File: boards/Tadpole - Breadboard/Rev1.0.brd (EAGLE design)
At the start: 57 x 50 mm, 8 parts

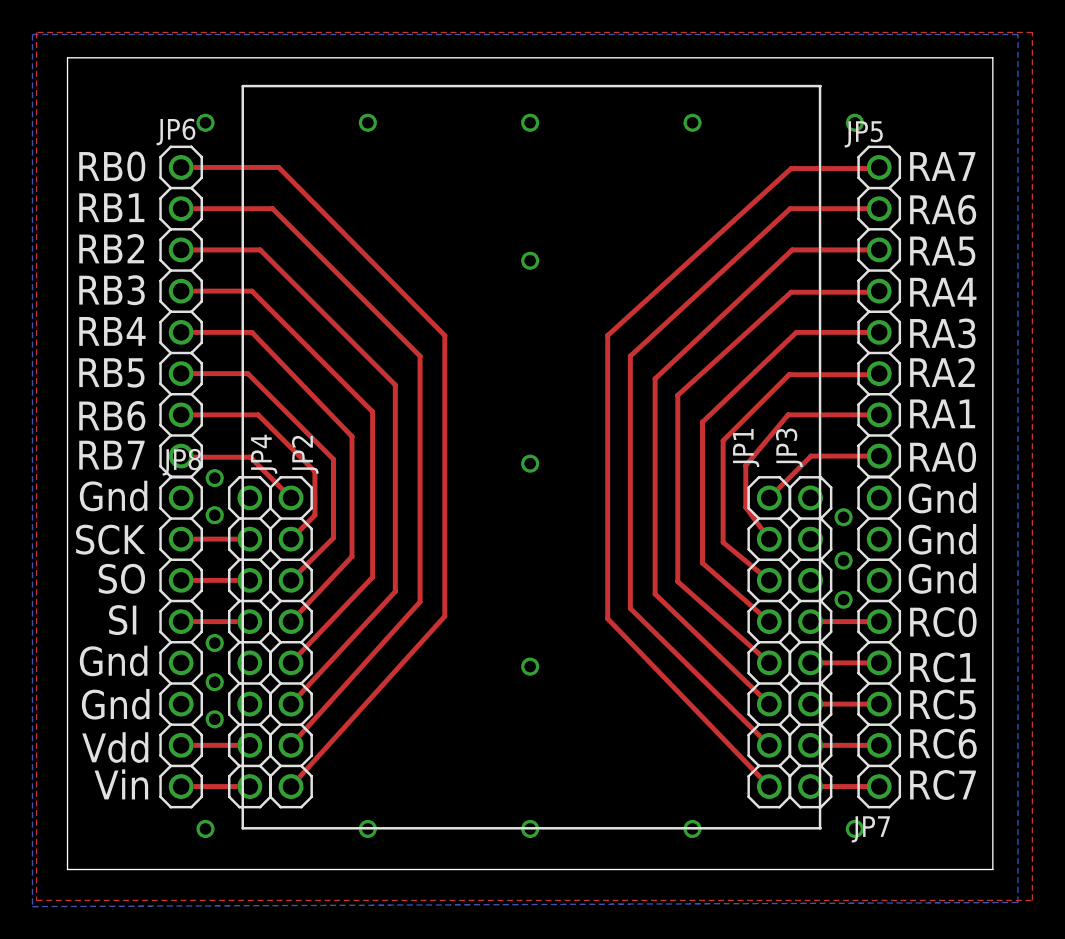
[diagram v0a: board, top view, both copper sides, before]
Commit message: Kermit PIC protocol and small frogbrain board mods.
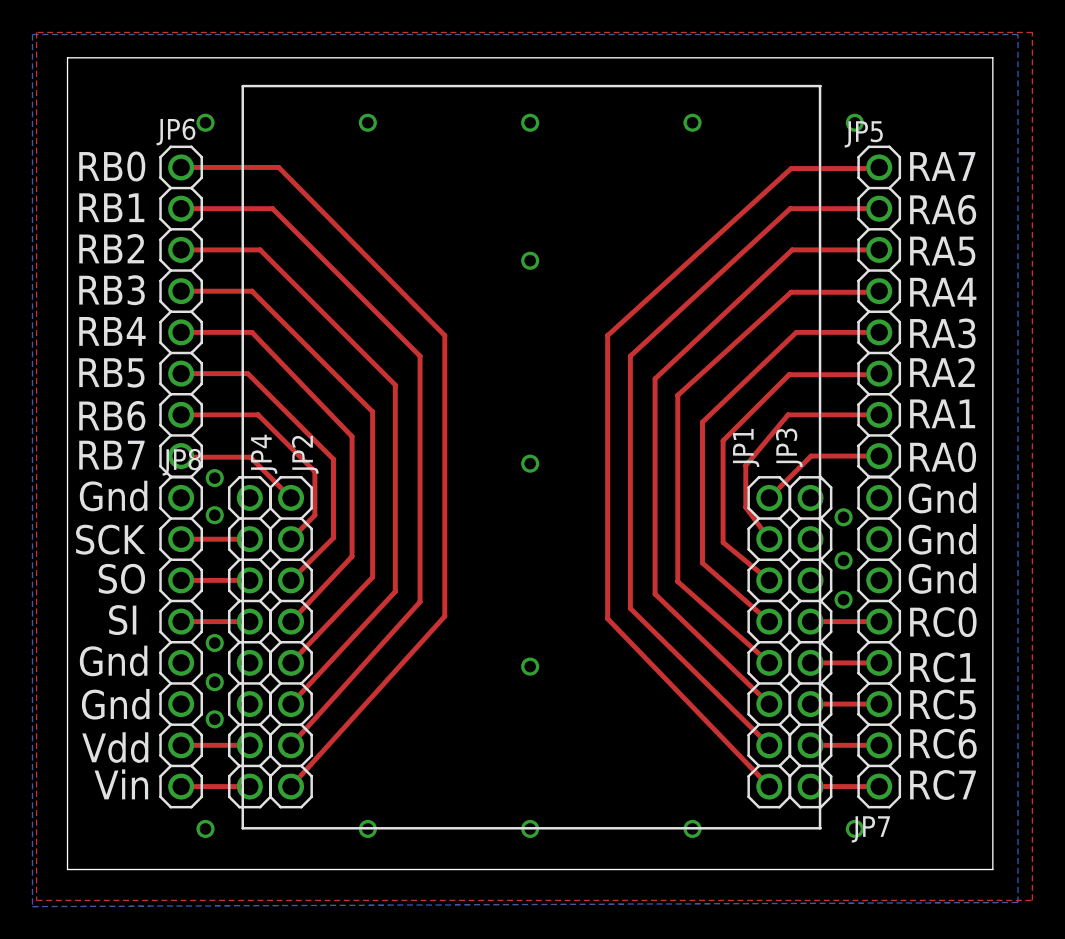
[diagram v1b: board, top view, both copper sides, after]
